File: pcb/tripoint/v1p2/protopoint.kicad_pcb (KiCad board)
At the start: 4 copper layers, 31.8 x 27.5 mm, 52 parts, among them T1 HHM1595A1, U1 STM32F031G6U6, U2 LXDC2HL, U3 DW1000, U4 SKY13317, U5 ProtoPoint_Module, X1 38.4M, X2 16M

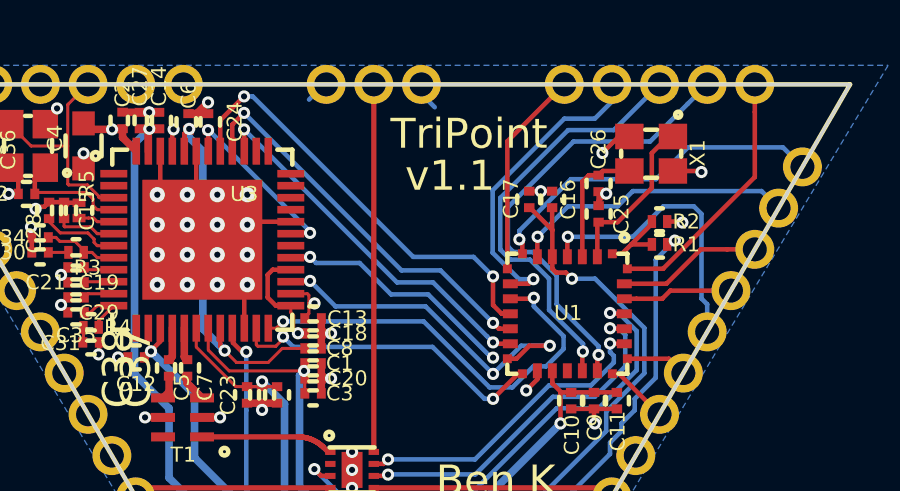
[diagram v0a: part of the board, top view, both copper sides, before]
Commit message: small changes to v1p2 board (cosmetic)
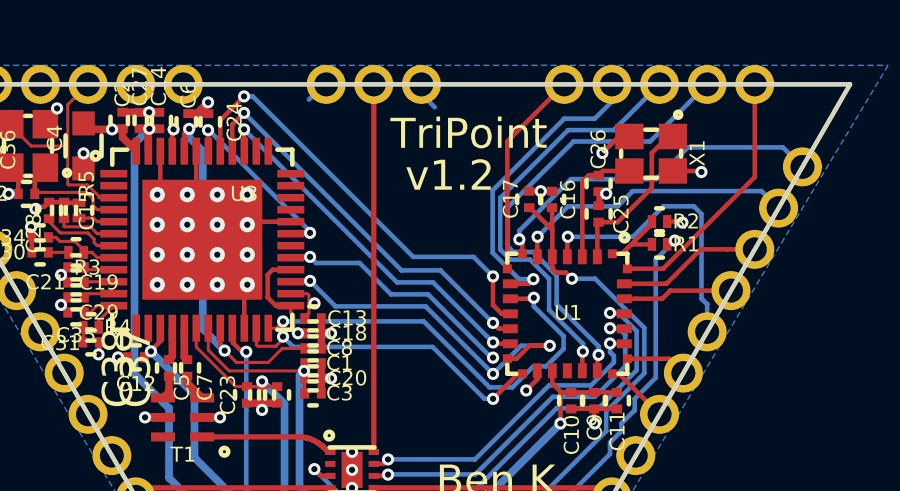
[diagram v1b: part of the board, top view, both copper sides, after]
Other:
- board text added: "v1.2"
- board text removed: "v1.1"
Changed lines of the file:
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@@
-(kicad_pcb (version 4) (host pcbnew "(2015-07-14 BZR 5941, Git c6c8b11)-product")
+(kicad_pcb (version 4) (host pcbnew 0.201509030901+6151~29~ubuntu15.04.1-product)
   (general
     (links 170)
@@
       (plotinvisibletext false)
       (padsonsilk false)
-      (subtractmaskfromsilk false)
+      (subtractmaskfromsilk true)
       (outputformat 1)
       (mirror false)
@@
     )
   )
-  (gr_text v1.1 (at 43.815 28.448) (layer F.SilkS)
+  (gr_text v1.2 (at 43.815 28.448) (layer F.SilkS)
     (effects (font (size 1 1) (thickness 0.2)))
   )
@@
   (segment (start 32.0564 29.977) (end 31.9344 29.855) (width 0.1016) (layer F.Cu) (net 21))
   (segment (start 31.9344 29.855) (end 31.7666 29.855) (width 0.1016) (layer F.Cu) (net 21))
-  (segment (start 35.55 37.15) (end 38.755026 37.15) (width 0.1778) (layer F.Cu) (net 22) (status 800000))
-  (segment (start 39.579007 37.479517) (end 39.599998 37.499999) (width 0.1778) (layer F.Cu) (net 22) (status C00000))
-  (segment (start 39.55752 37.459556) (end 39.579007 37.479517) (width 0.1778) (layer F.Cu) (net 22) (status C00000))
-  (segment (start 39.535549 37.440128) (end 39.55752 37.459556) (width 0.1778) (layer F.Cu) (net 22) (status 400000))
+  (segment (start 35.55 37.15) (end 38.755026 37.15) (width 0.1778) (layer F.Cu) (net 22))
+  (segment (start 39.579007 37.479517) (end 39.599998 37.499999) (width 0.1778) (layer F.Cu) (net 22))
+  (segment (start 39.55752 37.459556) (end 39.579007 37.479517) (width 0.1778) (layer F.Cu) (net 22))
+  (segment (start 39.535549 37.440128) (end 39.55752 37.459556) (width 0.1778) (layer F.Cu) (net 22))
   (segment (start 39.513108 37.421246) (end 39.535549 37.440128) (width 0.1778) (layer F.Cu) (net 22))
   (segment (start 39.49021 37.40292) (end 39.513108 37.421246) (width 0.1778) (layer F.Cu) (net 22))
